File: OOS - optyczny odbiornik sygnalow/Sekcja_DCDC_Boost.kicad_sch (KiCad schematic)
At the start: 10 parts, among them U3 AP3015KTR-G1

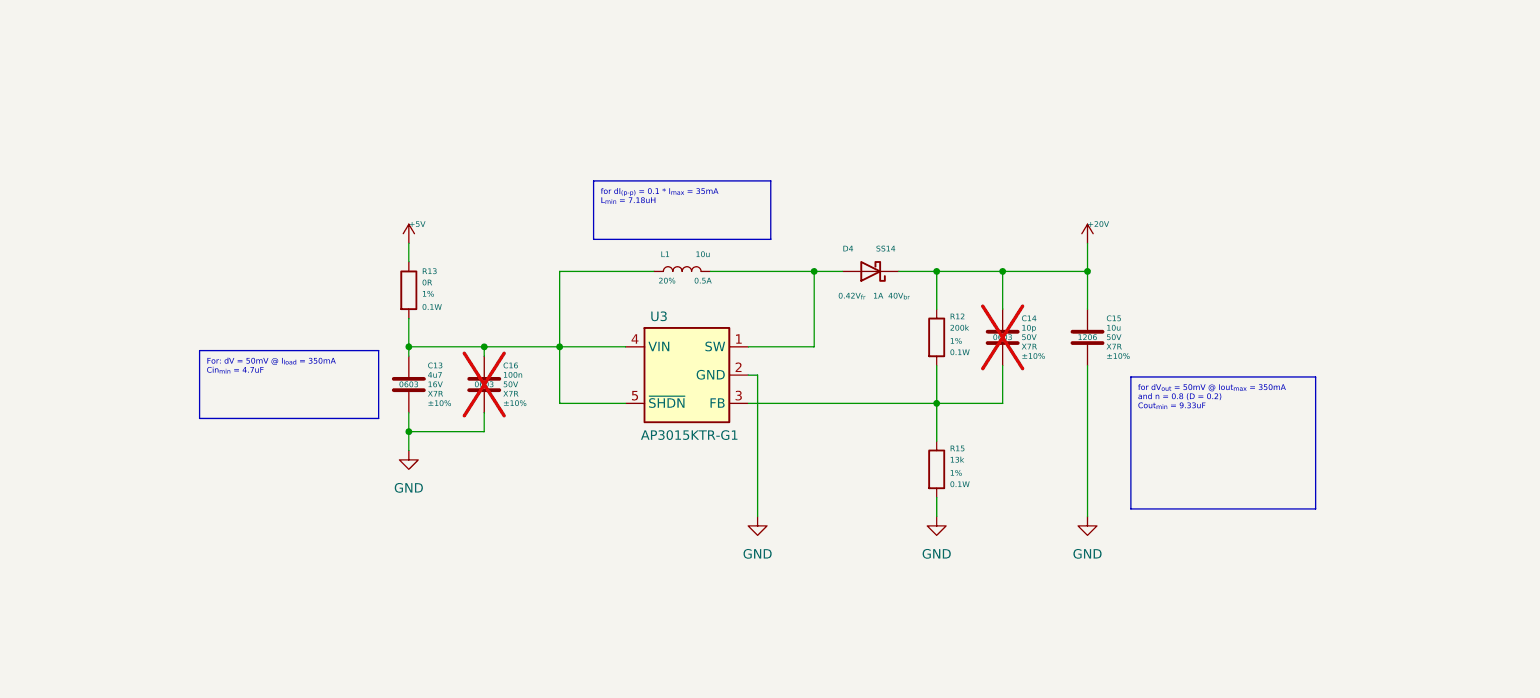
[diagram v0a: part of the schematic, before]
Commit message: Przeniesienie zmian z brancha Filip na review ze schematu Sekcja_DCDC_Boost
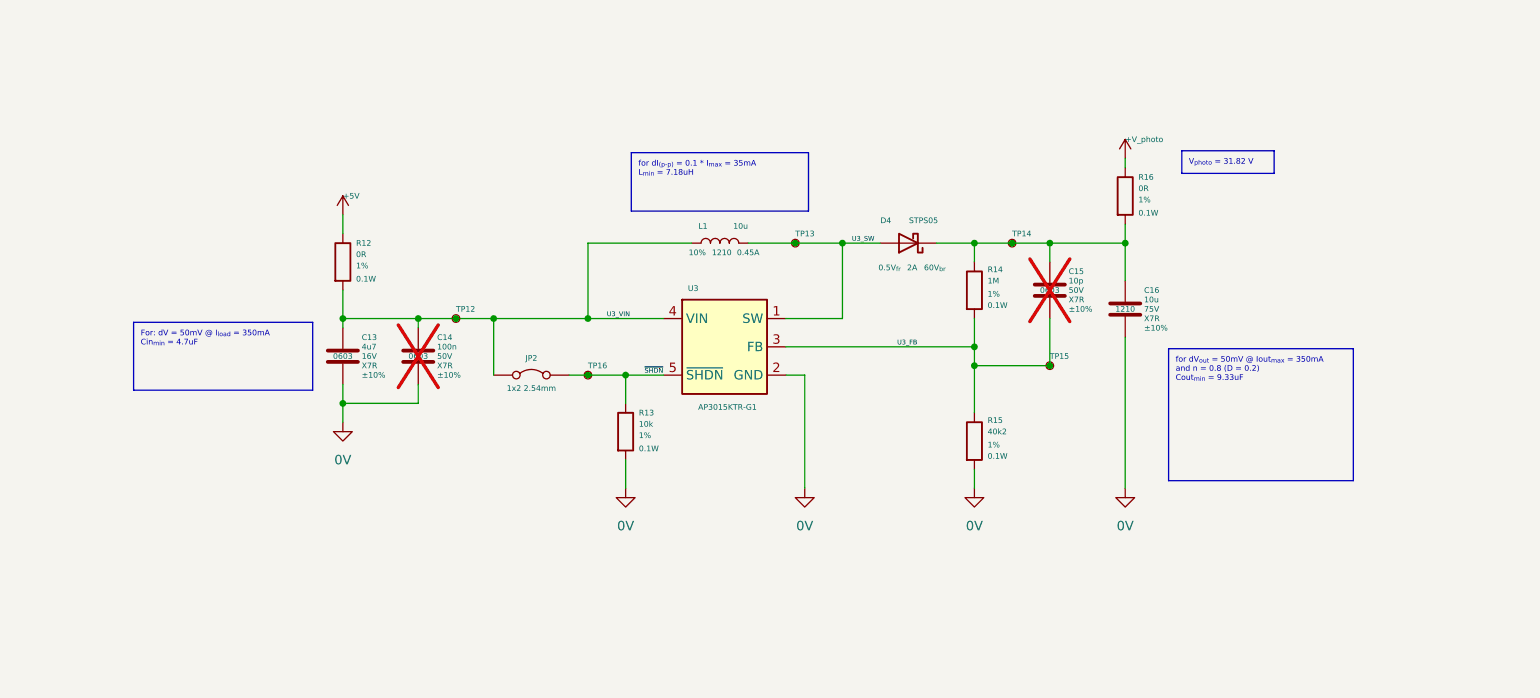
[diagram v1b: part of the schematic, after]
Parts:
- added JP2: 1x2 2.54mm, Connector_PinHeader_2.54mm:PinHeader_1x02_P2.54mm_Vertical, symbol Jumper:Jumper_2_Bridged
- added R13: 10k, Resistor_SMD:R_0603_1608Metric, symbol Device:R
- added R16: 0R, Resistor_SMD:R_0603_1608Metric, symbol Device:R
- added TP12, TP13, TP14, TP15, TP16: TestPoint_Small, TestPoint:TestPoint_Pad_D1.0mm, symbol Connector:TestPoint_Small
- C16: renamed from C15; footprint Capacitor_SMD:C_0603_1608Metric -> Capacitor_SMD:C_1210_3225Metric_Pad1.33x2.70mm_HandSolder; MPN  CL31B106KBHNNNE -> CGA6P1X7R1N106K250AC; Package 1206 -> 1210; Supplier Link https://www.tme.eu/pl/en/details/cl31b106kbhnnne/mlcc-smd-c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 -> https://www.tme.eu/pl/en/details/cga6p1x7r1n106kac/mlcc-smd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; Voltage Rating 50V -> 75V
- D4: value SS14 -> STPS05; footprint Diode_SMD:D_SMA -> Diode_SMD:Nexperia_CFP3_SOD-123W; Current 1A -> 2A; Forward V 0.42V_{fr} -> 0.5V_{fr}; MPN SS14L_R1_00001 -> STPS0560Z; Package SMA -> SOD123; Reverse V 40V_{br} -> 60V_{br}; Supplier link https://www.tme.eu/pl/en/details/ss14l-r1/smd-schottky-diod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 -> https://www.tme.eu/pl/en/details/stps0560z/smd-schottky-dio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
- L1: footprint Inductor_SMD:L_0805_2012Metric_Pad1.05x1.20mm_HandSolder -> Inductor_SMD:L_1210_3225Metric_Pad1.42x2.65mm_HandSolder; Current 0.5A -> 0.45A; MPN MLZ2012N100LTD25 -> NLCV32T-100K-EF; Package 0805 -> 1210; Supplier link https://www.tme.eu/pl/en/details/mlz2012n100ltd25/inductors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 -> https://www.tme.eu/pl/en/details/nlcv32t-100k-ef/inductors/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; Tolerance 20% -> 10%
- R14: renamed from R12; value 200k -> 1M; MPN WR06X2003FTL -> CRCW06031M00FKEA; Supplier link https://www.tme.eu/pl/details/wr06x2003ftl/rezystory-smd/wa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 -> https://www.tme.eu/pl/en/details/crcw06031m00fkea/smd-resis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
- R15: value 13k -> 40k2; MPN ERJ3EKF1302V -> ERJ3EKF4022V; Supplier link https://www.tme.eu/pl/details/erj3ekf1302v/rezystory-smd/pa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 -> https://www.tme.eu/pl/en/details/erj3ekf4022v/smd-resistors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
- renumbered C16 to C14, C14 to C15, R13 to R12
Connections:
- net U3_FB: now reaches C15.2, R14.2, R15.1, U3.3 (FB)
- net U3_FB: now also TP15.1
- net U3_SW: now reaches D4.2 (A), L1.2, U3.1 (SW)
- net U3_SW: now also TP13.1
- net U3_VIN: now reaches C13.1, C14.1, L1.1, R12.2, U3.4 (VIN)
- net U3_VIN: now also JP2.1 (A), TP12.1; no longer U3.5 (~{SHDN})
- net +20V: no longer names the net of C15.1, C16.1, D4.1 (K), R14.1
- net +20V: now also R16.2, TP14.1
- net GND renamed 0V
- net 0V: now also R13.2
- new net +V_photo: R16.1
- new net ~{SHDN}: JP2.2 (B), R13.1, TP16.1, U3.5 (~{SHDN})
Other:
- moved on the sheet: C13, C14, C15, C16, D4, L1, R12, R14, R15, U3

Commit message: Solved points from review on page OOS - Analog
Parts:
- C13: MPN  GRM188Z71C475KE21D -> (none)
- C14: MPN CGA3E2X7R1H104K080AA -> (none)
- C15: MPN 06035C100KAT2A -> (none)
- C16: MPN  CGA6P1X7R1N106K250AC -> (none)
- D4: Current 2A -> (none); Forward V 0.5V_{fr} -> (none); MPN STPS0560Z -> (none); Reverse V 60V_{br} -> (none); Supplier link https://www.tme.eu/pl/en/details/stps0560z/smd-schottky-dio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 -> (none)
- L1: Current 0.45A -> (none); MPN NLCV32T-100K-EF -> (none); Supplier link https://www.tme.eu/pl/en/details/nlcv32t-100k-ef/inductors/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 -> (none)
- R12, R16: MPN CRCW06030000Z0EA -> (none)
- R13: MPN AC0603FR-0710KL -> (none)
- R14: MPN CRCW06031M00FKEA -> (none); Supplier link https://www.tme.eu/pl/en/details/crcw06031m00fkea/smd-resis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 -> (none)
- R15: MPN ERJ3EKF4022V -> (none); Supplier link https://www.tme.eu/pl/en/details/erj3ekf4022v/smd-resistors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 -> (none)
- U3: MPN AP3015KTR-G1 -> (none); Supplier link https://www.tme.eu/pl/details/ap3015ktr-g1/regulatory-napie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 -> (none)
